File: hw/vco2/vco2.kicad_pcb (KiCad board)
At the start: 2 copper layers, 60 x 110 mm, 139 parts, among them J1 Conn_02x08_Odd_Even, Q1 DNP, U1 SSI2131, U2 TL431BCDBZ, U3 TL072HxD, U4 TL072HxD, U5 TL072HxD, U6 TL431BCDBV, U7 TL072HxD, U8 TL072HxD, U9 SSI2131

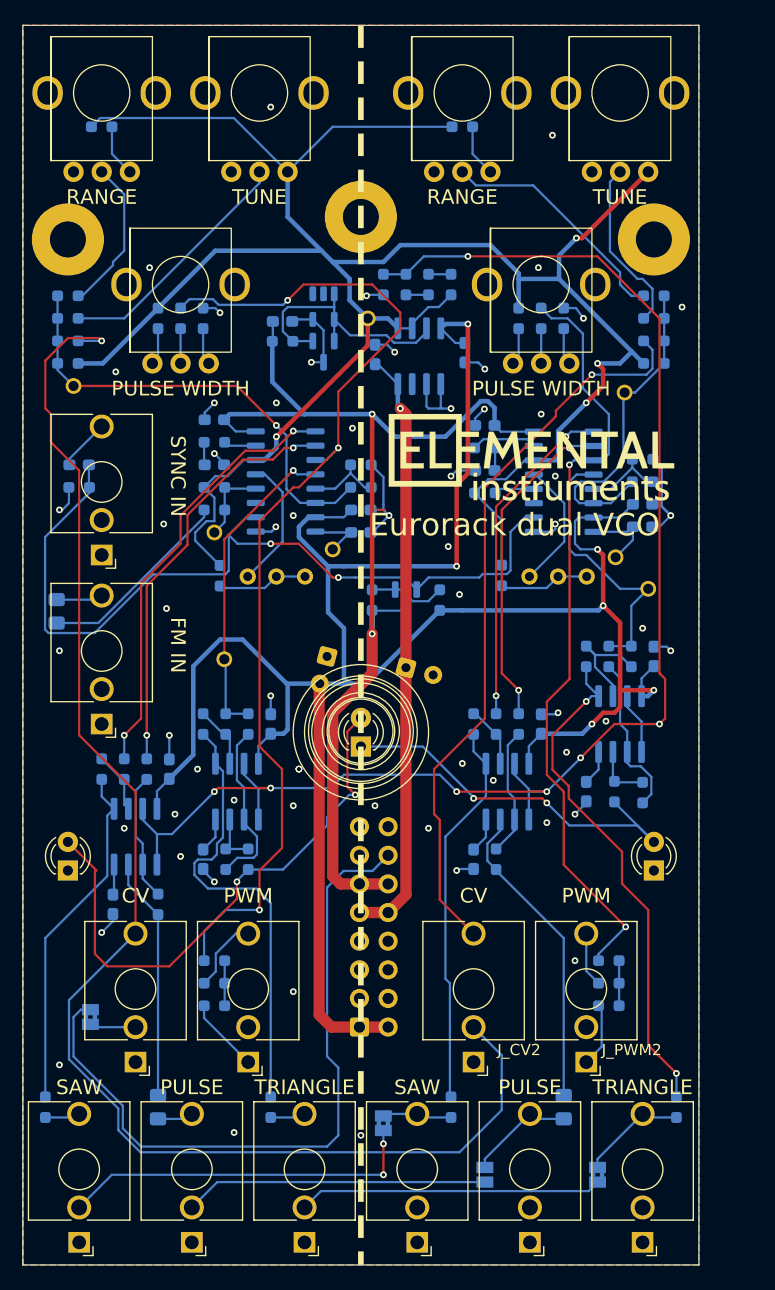
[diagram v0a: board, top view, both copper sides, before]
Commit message: Tiny fixes to PCB layout
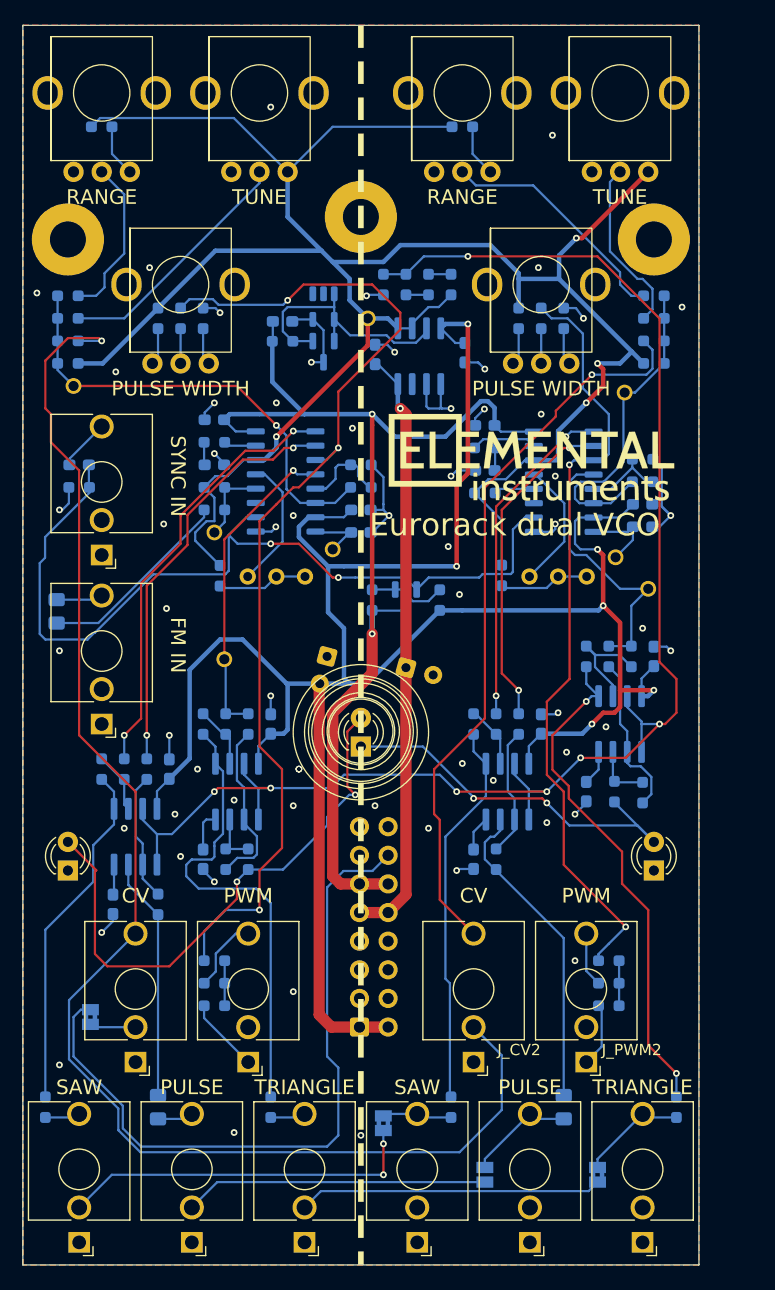
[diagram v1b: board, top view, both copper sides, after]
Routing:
- net ANTI_HANGUP: track 74.9 -> 76.5 mm
- net Net-(R5-Pad1): track 40.0 -> 41.4 mm
- net OPREF: track 140.0 -> 141.1 mm
- net /Oscillator 1/HF_TRACK: track 6.77 -> 7.67 mm
- net Net-(R17-Pad1): track 13.7 -> 14.5 mm
- net GND: track 83.0 -> 82.3 mm, vias 61 -> 62
